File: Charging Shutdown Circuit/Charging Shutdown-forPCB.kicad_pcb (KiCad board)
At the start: 2 copper layers, 177.8 x 127 mm, 21 parts, among them J1 in charger, J10 Button E-STOP, J11 SH-RESET, J13 TSMP (out), J3 120v DC (in), J4 Out of Charger, J6 Temp Sensor, J7 AC in this world!, J8 DC out of this world!, K1 Charger Contactor +, K2 Charger Contactor -

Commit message: charger pbc for suree
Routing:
- net +12V: track 61.9 -> 57.5 mm, vias 2 -> 0
- net /Shutdown_Final: track 58.2 -> 60.9 mm, vias 2 -> 1
- net GND: track 83.8 -> 82.8 mm
- net /Charge_State: vias 0 -> 1
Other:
- board text added: "12V"
- board text added: "Charge Enable"
- board text added: "Charge State SH_Reset"
- board text added: "GLV"
- board text added: "GND"
- board text added: "SH_Reset"
- board text added: "Shutdown Acc_IN"
- board text added: "Shutdown Final"
- board text added: "TS +"
- board text added: "TS -"
- board text added: "TSMP +"
- board text added: "TSMP -"
- board text added: "Temp Sensor"
- board text added: "Tractive System"
- board text removed: "GLV Tractive System"

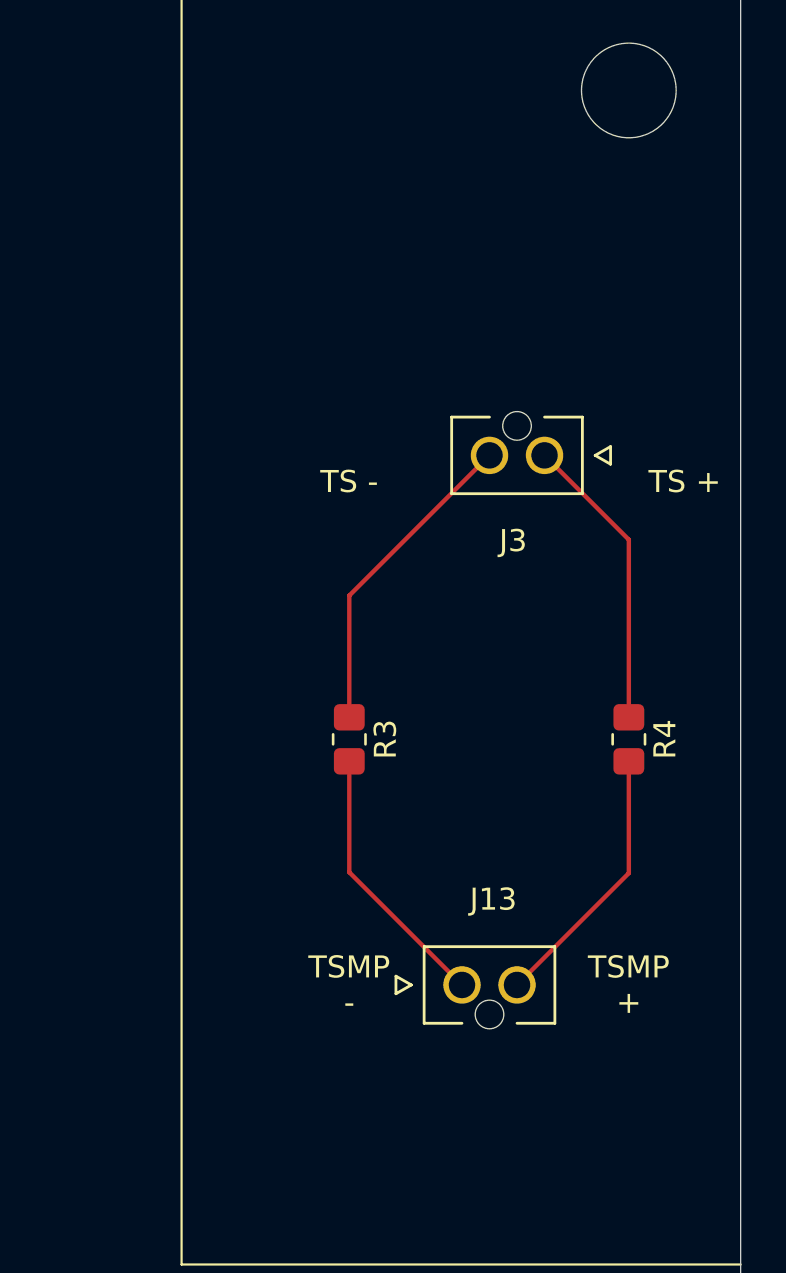
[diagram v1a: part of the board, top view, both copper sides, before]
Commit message: fixing charger pcb from sam's comments
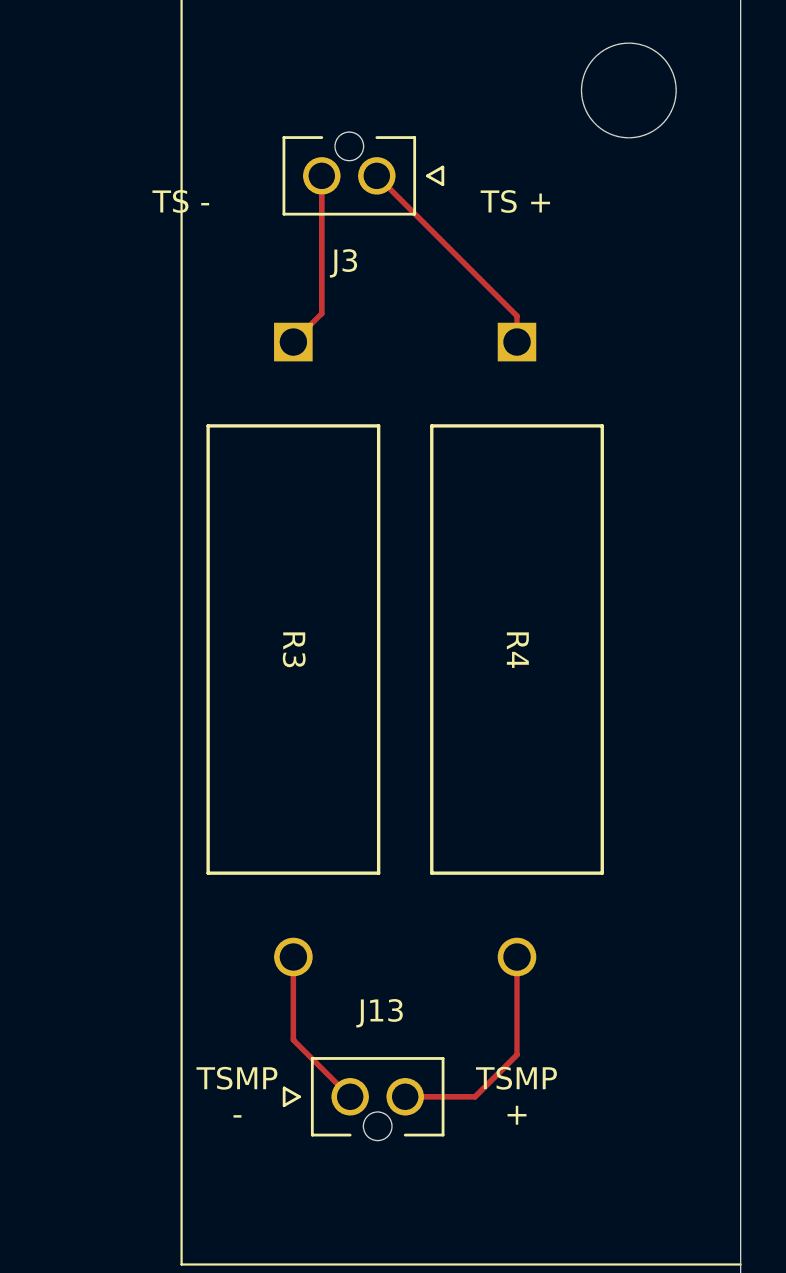
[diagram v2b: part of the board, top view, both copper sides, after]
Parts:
- R3, R4: footprint Resistor_SMD:R_0805_2012Metric_Pad1.20x1.40mm_HandSolder -> 1FS_2_Global_Footprint_Library:RES_WH&slash_NE_OHM
- moved R4 18.8 mm to (180.3, 29.2)
- moved R3 18.2 mm to (170.2, 29.2)
- moved J3 14.8 mm to (174.0, 21.7)
- moved J13 7.18 mm to (172.8, 63.5)
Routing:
- net Net-(J3-Pad2): track 14.5 -> 8.08 mm
- net Net-(J13-Pad1): track 12.3 -> 7.42 mm
- net Net-(J3-Pad1): track 13.5 -> 10.2 mm
- net Net-(J13-Pad2): track 12.3 -> 10.3 mm
